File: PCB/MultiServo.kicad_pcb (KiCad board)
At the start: 2 copper layers, 70 x 34 mm, 57 parts, among them J1 USB_B_Mini, J2 S04B, J3 DB9_M, Q1 16MHz, U1 FT230XS, U10 SN74LV1T126, U11 SN74LVC1G86, U2 Si8621BC, U3 ATSAMC21E18A-MUT, U4 MP2456GJ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

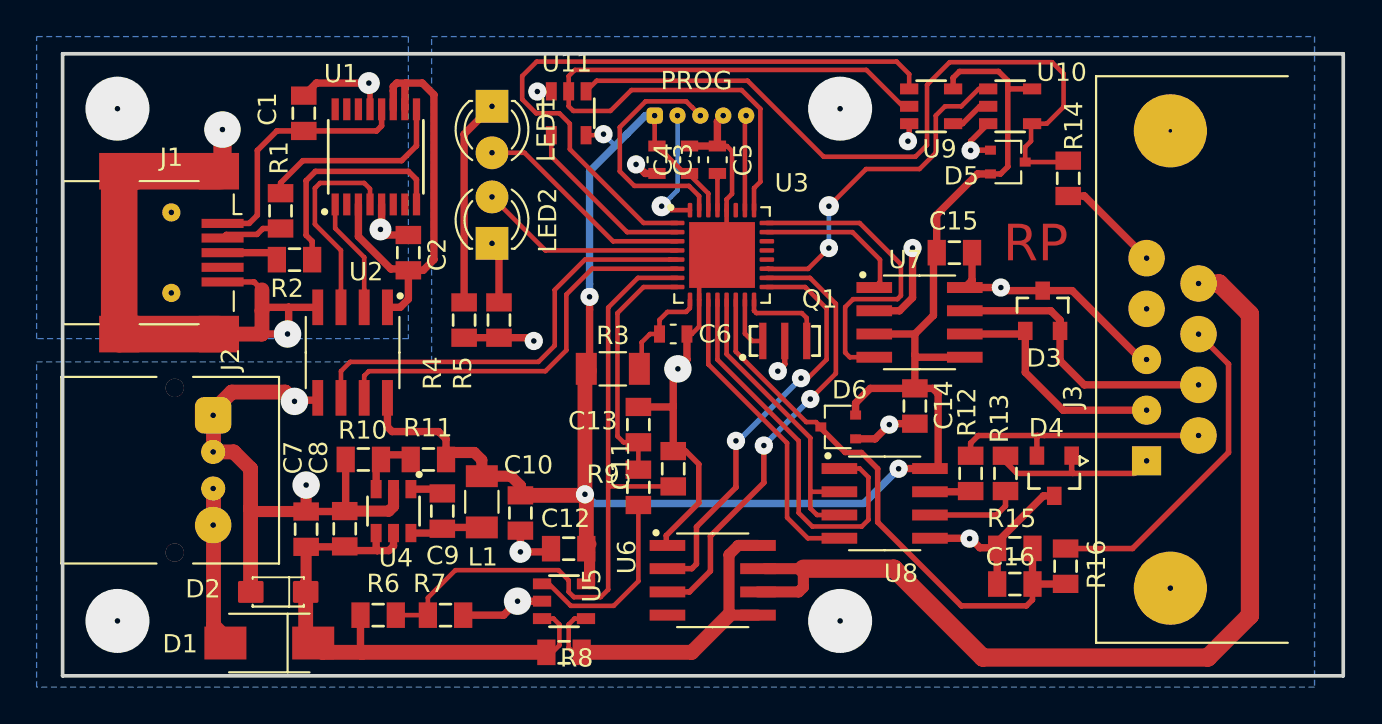
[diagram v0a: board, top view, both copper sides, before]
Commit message: KeeLoq is working now CAN is also working
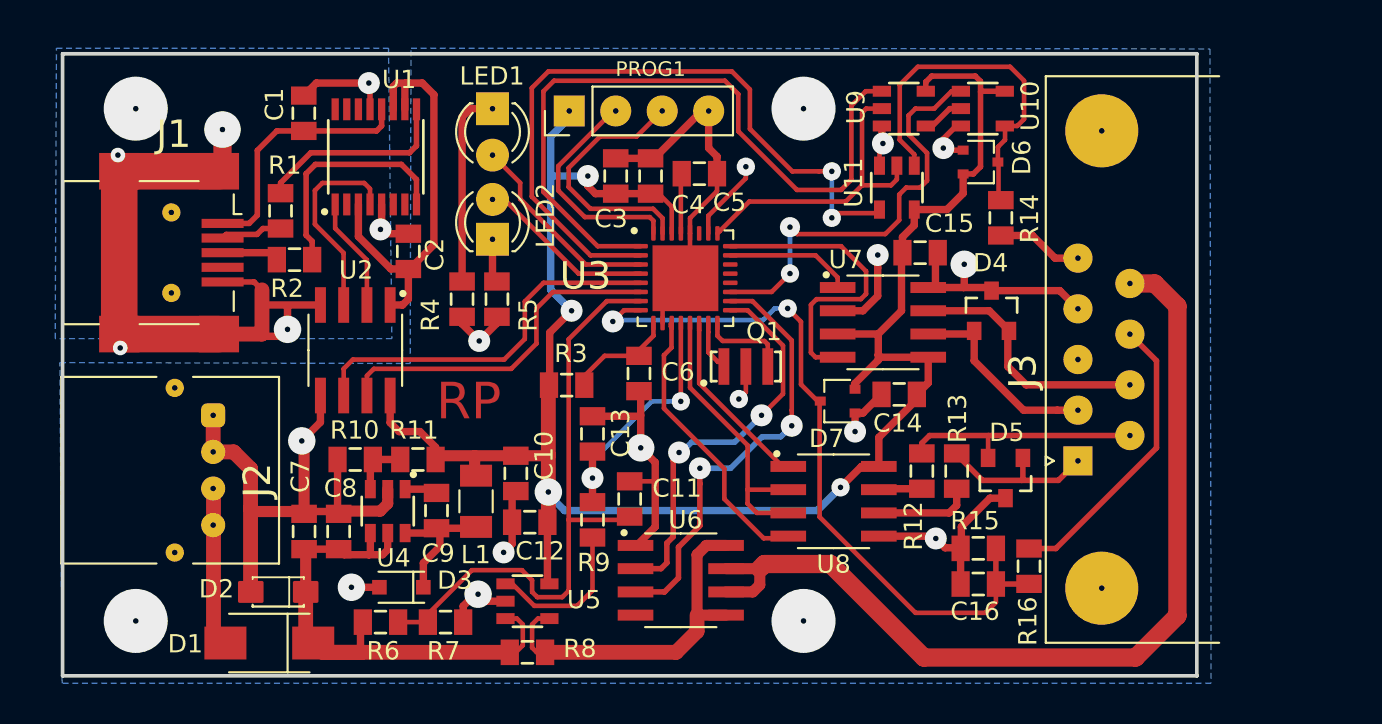
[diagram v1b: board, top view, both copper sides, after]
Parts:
- removed PROG: SW, VolzLib:Conn_ARM_1x05
- added D7: BAT54SW, VolzLib:SOT-323_SC-70, F.Cu at (112.4, 119.0)
- added PROG1: 01x04, Connector_PinHeader_2.54mm:PinHeader_1x04_P2.54mm_Vertical, F.Cu at (97.7, 103.1)
- C3, C4, C5, C6: footprint VolzLib:C0603 -> VolzLib:C0805
- D3: value NUP2105L -> BAT165; footprint VolzLib:SOT23-3 -> VolzLib:D_SOD-323
- D5: value BAT54SW -> NUP2105L; footprint VolzLib:SOT-323_SC-70 -> VolzLib:SOT23-3
- R3: footprint VolzLib:R1206 -> VolzLib:R0805
- moved D3 38.2 mm to (88.5, 129.2), turned to 180 degrees
- moved U11 18.4 mm to (115.6, 107.3)
- moved D5 17.3 mm to (121.5, 123.2), turned to 180 degrees
- moved D6 16.4 mm to (120.2, 105.9), turned to 0 degrees
- moved D4 9.65 mm to (120.8, 114.0), turned to 0 degrees
- moved R14 4.27 mm to (121.3, 109.0)
- moved J3 3.75 mm to (125.5, 122.2)
- moved R9 3.07 mm to (99.0, 125.5)
- moved C11 2.90 mm to (101.0, 124.3)
- moved C6 2.86 mm to (101.5, 117.5), turned to 270 degrees
- moved U8 2.80 mm to (112.1, 124.5)
- moved R3 2.68 mm to (97.6, 118.1), turned to 180 degrees
- moved R12 2.67 mm to (117.0, 122.8)
- moved R13 2.67 mm to (118.9, 122.8)
- moved C12 2.57 mm to (95.5, 125.6)
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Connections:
- net /PWM_P renamed Net-(U3-Pad20)
- net /PWM_RX renamed Net-(U3-Pad21)
- net /PWM_TX renamed Net-(U3-Pad22)
- C16 pad 2: /ADC__FB -> /ADC_FB
- D3 pad 1: /CANL -> Net-(C9-Pad2)
- D3 pad 2: /CANH -> GND
- D4 pad 1: /485_A -> /CANL
- D4 pad 2: /485_B -> /CANH
- D5 pad 1: GND -> /485_A
- D5 pad 2: +5V -> /485_B
- D5 pad 3: Net-(D5-Pad3) -> GND
- D6 pad 3: /ADC__FB -> Net-(D6-Pad3)
- R14 pad 2: Net-(D5-Pad3) -> Net-(D6-Pad3)
- R15 pad 2: /ADC__FB -> /ADC_FB
- R16 pad 2: /ADC__FB -> /ADC_FB
- R3 pad 1: +5V -> Net-(C6-Pad1)
- R3 pad 2: Net-(C6-Pad1) -> +5V
- U10 pad 4: Net-(D5-Pad3) -> Net-(D6-Pad3)
- U11 pad 1: Net-(D5-Pad3) -> Net-(D6-Pad3)
- U3 pad : GND -> (no net)
- U3 pad 12: /485_RX -> /ADC_I
- U3 pad 14: /ADC__FB -> /485_RX
- U3 pad 8: /ADC_I -> /ADC_FB
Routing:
- net Net-(D5-Pad3): track 40.9 -> 0.00 mm
- net /ADC_FB: track 0.00 -> 40.6 mm, vias 0 -> 2
- net /ADC__FB: track 31.3 -> 0.00 mm
- net /SBUSRX: track 9.75 -> 38.8 mm, vias 0 -> 2
- net /SBUSPOL: track 38.4 -> 16.9 mm
- net Net-(D6-Pad3): track 0.00 -> 19.8 mm
- net /485_RX: track 21.9 -> 10.0 mm
- net /SWDIO: track 6.98 -> 12.3 mm, vias 1 -> 0
- net /SBUSTE: track 18.7 -> 23.3 mm
- net +5V: track 110.9 -> 106.3 mm
- net /ADC_U: track 37.8 -> 33.8 mm
- net /USB_RX: track 22.8 -> 19.1 mm
- net /USB_TX: track 24.3 -> 20.8 mm
- net Net-(C9-Pad2): track 4.26 -> 7.69 mm
- net /SBUSTX: track 35.9 -> 39.1 mm
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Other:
- board size 70 x 34 mm -> 62 x 34 mm
